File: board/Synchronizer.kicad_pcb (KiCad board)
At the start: 2 copper layers, 99 x 61 mm, 46 parts, among them J1 Conn_01x02_Socket, J2 COIL1, J3 COIL2, Q1 2N3904, Q2 2N3906, Q3 IRF9540N, Q4 2N3904, U1 Pico, U2 LM7805_TO220, U3 LM358

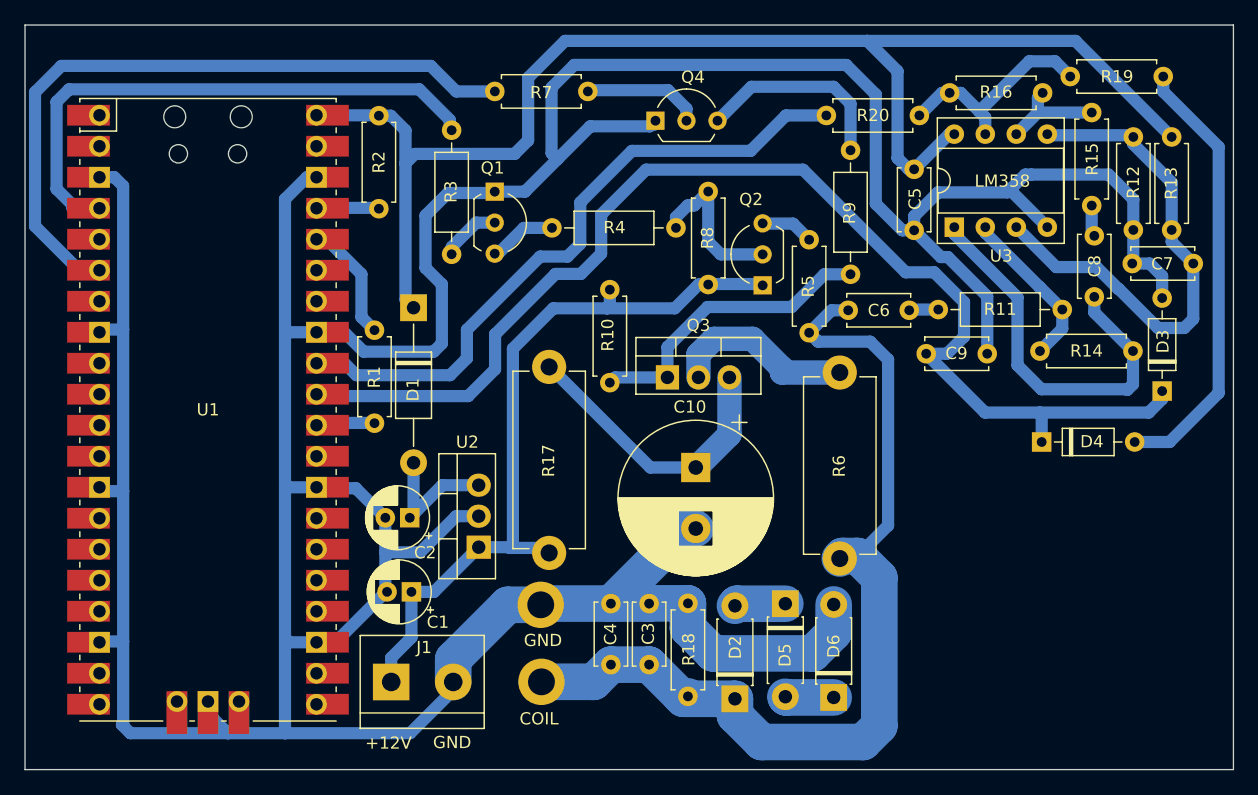
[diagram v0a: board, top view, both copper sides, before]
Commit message: Added pcb2gcode generation of gcode for mill
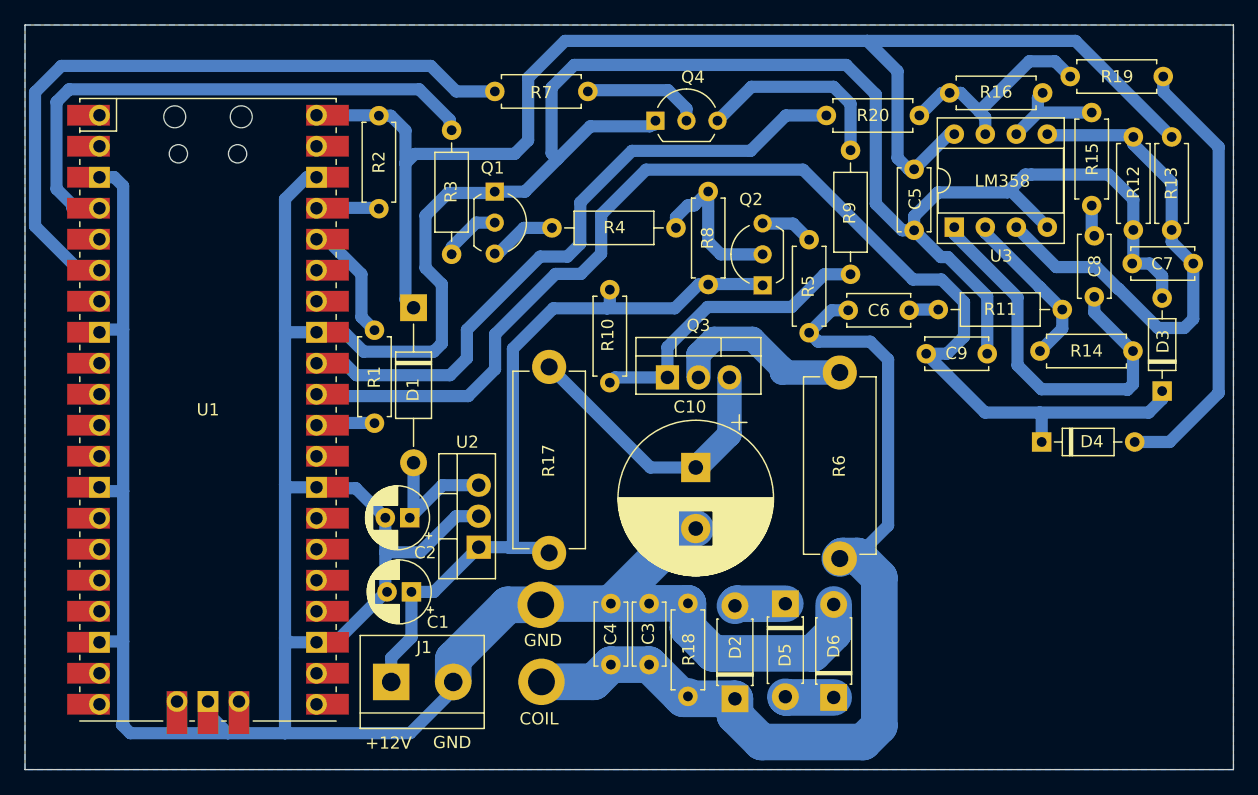
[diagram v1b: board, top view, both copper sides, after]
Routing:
- added copper zone on B.Cu, net (none)
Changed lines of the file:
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@@
   (segment (start 178.6 44.54) (end 181.77 47.71) (width 1) (layer "B.Cu") (net 9))
   (segment (start 181.77 50.43) (end 181.77 47.71) (width 1) (layer "B.Cu") (net 9))
-  (segment (start 134.46 41.39) (end 129.51 46.34) (width 1) (layer "B.Cu") (net 10))
-  (segment (start 129.51 46.34) (end 129.51 49.2) (width 1) (layer "B.Cu") (net 10))
+  (segment (start 115.03 51.4) (end 114.88 51.25) (width 1) (layer "B.Cu") (net 10))
   (segment (start 166.53 47.93) (end 167.93 46.53) (width 1) (layer "B.Cu") (net 10))
+  (segment (start 129.51 49.2) (end 127.31 51.4) (width 1) (layer "B.Cu") (net 10))
+  (segment (start 167.93 46.53) (end 167.93 43.7) (width 1) (layer "B.Cu") (net 10))
+  (segment (start 141.88 32.85) (end 138.2 36.53) (width 1) (layer "B.Cu") (net 10))
+  (segment (start 163.74 41.85) (end 154.74 32.85) (width 1) (layer "B.Cu") (net 10))
   (segment (start 164.83 47.93) (end 166.53 47.93) (width 1) (layer "B.Cu") (net 10))
-  (segment (start 115.03 51.4) (end 114.88 51.25) (width 1) (layer "B.Cu") (net 10))
-  (segment (start 127.31 51.4) (end 115.03 51.4) (width 1) (layer "B.Cu") (net 10))
   (segment (start 174.13 52.75) (end 169.65 52.75) (width 1) (layer "B.Cu") (net 10))
-  (segment (start 165.49 41.26) (end 163.15 41.26) (width 1) (layer "B.Cu") (net 10))
+  (segment (start 154.74 32.85) (end 141.88 32.85) (width 1) (layer "B.Cu") (net 10))
+  (segment (start 138.2 36.53) (end 138.2 39.73) (width 1) (layer "B.Cu") (net 10))
   (segment (start 169.65 52.75) (end 164.83 47.93) (width 1) (layer "B.Cu") (net 10))
-  (segment (start 154.74 32.85) (end 141.88 32.85) (width 1) (layer "B.Cu") (net 10))
-  (segment (start 167.93 43.7) (end 165.49 41.26) (width 1) (layer "B.Cu") (net 10))
-  (segment (start 167.93 46.53) (end 167.93 43.7) (width 1) (layer "B.Cu") (net 10))
   (segment (start 183.06 52.75) (end 174.13 52.75) (width 1) (layer "B.Cu") (net 10))
   (segment (start 184.16 50.99) (end 184.16 51.65) (width 1) (layer "B.Cu") (net 10))
-  (segment (start 129.51 49.2) (end 127.31 51.4) (width 1) (layer "B.Cu") (net 10))
-  (segment (start 138.2 36.53) (end 138.2 39.73) (width 1) (layer "B.Cu") (net 10))
-  (segment (start 141.88 32.85) (end 138.2 36.53) (width 1) (layer "B.Cu") (net 10))
-  (segment (start 163.15 41.26) (end 154.74 32.85) (width 1) (layer "B.Cu") (net 10))
   (segment (start 138.2 39.73) (end 136.54 41.39) (width 1) (layer "B.Cu") (net 10))
+  (segment (start 136.54 41.39) (end 134.46 41.39) (width 1) (layer "B.Cu") (net 10))
+  (segment (start 129.51 46.34) (end 129.51 49.2) (width 1) (layer "B.Cu") (net 10))
+  (segment (start 134.46 41.39) (end 129.51 46.34) (width 1) (layer "B.Cu") (net 10))
   (segment (start 184.16 51.65) (end 183.06 52.75) (width 1) (layer "B.Cu") (net 10))
   (segment (start 174.29 52.91) (end 174.29 55.16) (width 1) (layer "B.Cu") (net 10))
+  (segment (start 167.93 43.7) (end 166.08 41.85) (width 1) (layer "B.Cu") (net 10))
   (segment (start 174.13 52.75) (end 174.29 52.91) (width 1) (layer "B.Cu") (net 10))
-  (segment (start 136.54 41.39) (end 134.46 41.39) (width 1) (layer "B.Cu") (net 10))
+  (segment (start 127.31 51.4) (end 115.03 51.4) (width 1) (layer "B.Cu") (net 10))
+  (segment (start 166.08 41.85) (end 163.74 41.85) (width 1) (layer "B.Cu") (net 10))
   (segment (start 148.71 49.87) (end 148.71 54.55) (width 2) (layer "B.Cu") (net 11))
   (segment (start 133.99 49.01) (end 133.94 49.01) (width 1) (layer "B.Cu") (net 11))
@@
   (segment (start 169.175 28.075) (end 167.66 26.56) (width 1) (layer "B.Cu") (net 57))
   (segment (start 169.67 28.57) (end 169.175 28.075) (width 1) (layer "B.Cu") (net 57))
+  (zone (net 0) (net_name "") (layer "B.Cu") (hatch edge 0.5)
+    (connect_pads (clearance 0.75))
+    (min_thickness 0.75) (filled_areas_thickness no)
+    (fill yes (thermal_gap 0.75) (thermal_bridge_width 0.75) (island_removal_mode 1) (island_area_min 10))
+    (polygon
+      (pts
+        (xy 91 21)
+        (xy 190 21)
+        (xy 190 82)
+        (xy 91 82)
+      )
+    )
+  )
 )

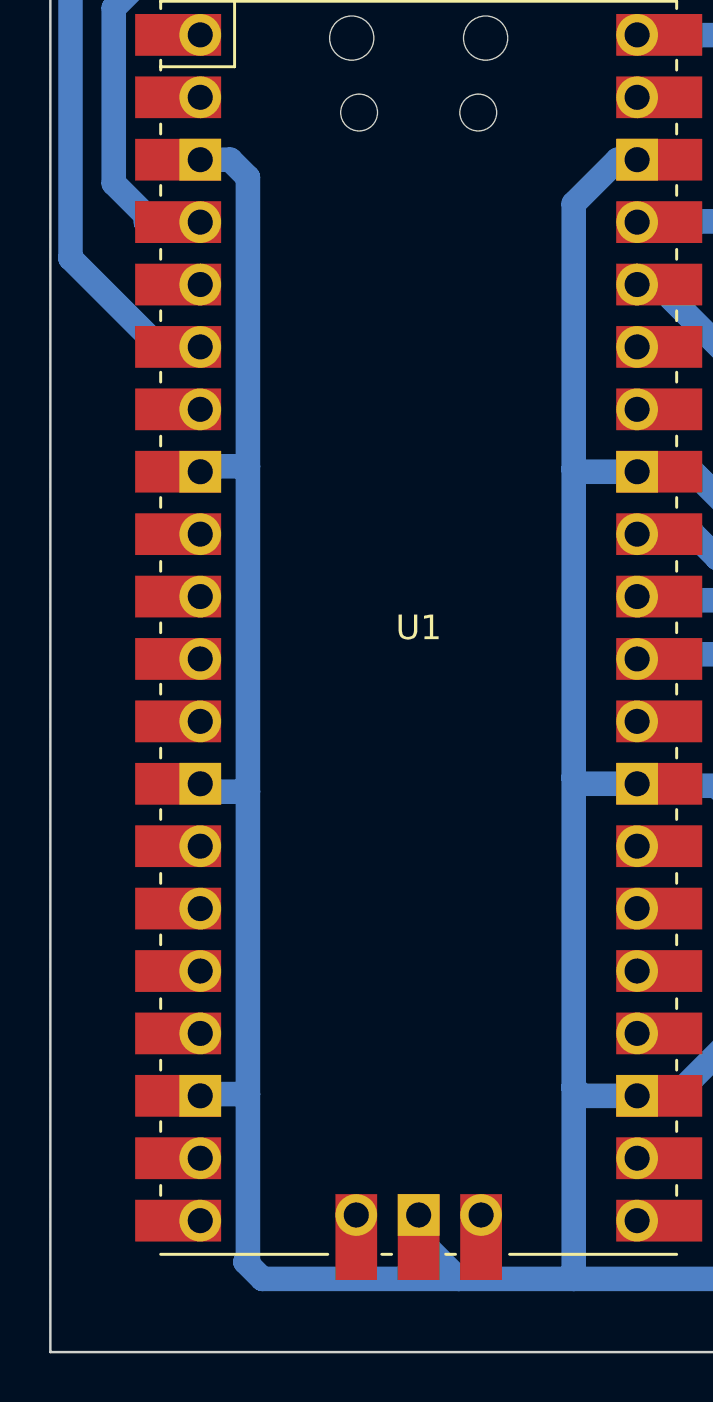
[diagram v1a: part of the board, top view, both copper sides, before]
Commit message: Added CAD of coil form
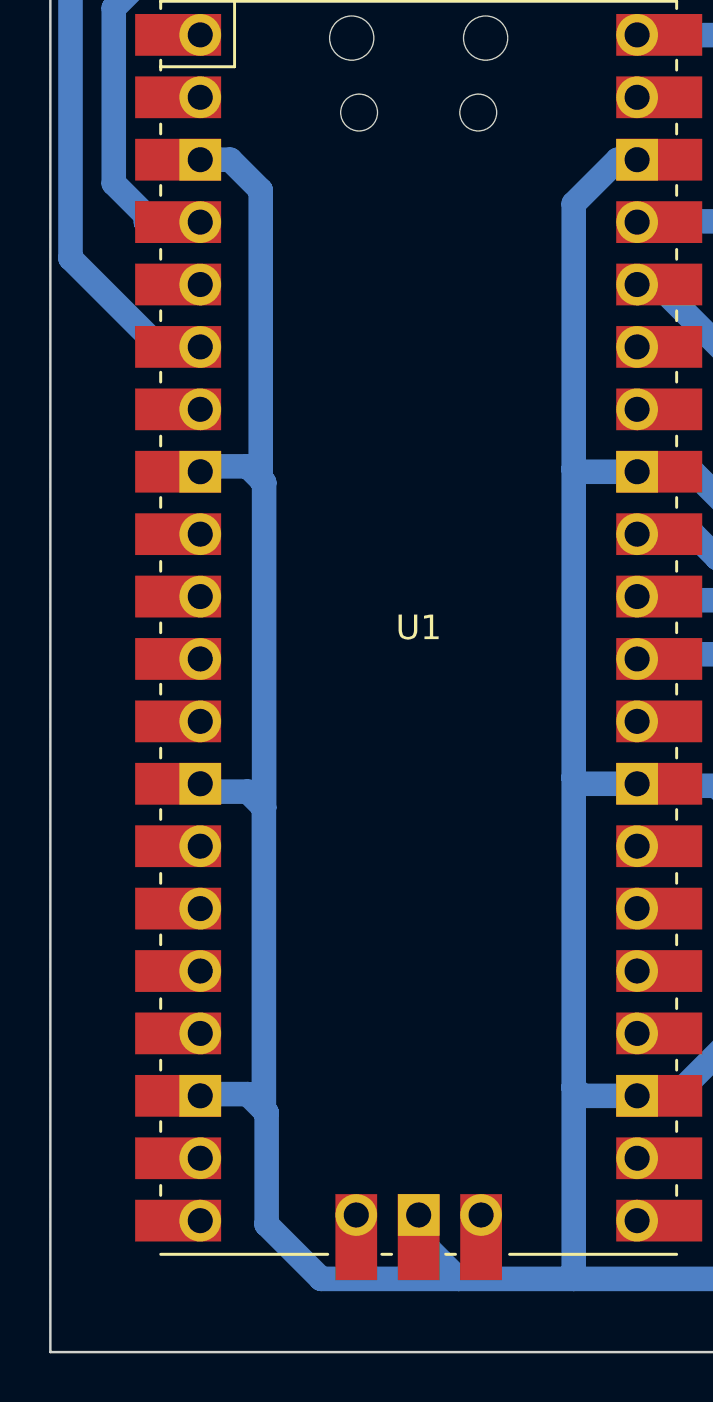
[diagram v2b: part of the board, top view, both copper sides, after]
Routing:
- net GND: track 360.6 -> 362.1 mm
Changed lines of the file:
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@@
   (segment (start 162.87 37.82) (end 163.84 37.82) (width 1) (layer "B.Cu") (net 2))
   (segment (start 137.31 29.3) (end 134.625 31.985) (width 1) (layer "B.Cu") (net 2))
-  (segment (start 99.04 78.23) (end 99.04 71.5) (width 1) (layer "B.Cu") (net 2))
   (segment (start 166.03 40.01) (end 163.84 37.82) (width 1) (layer "B.Cu") (net 2))
+  (segment (start 99.7 59.83) (end 99.7 46.61) (width 1) (layer "B.Cu") (net 2))
   (segment (start 169.83 47.93) (end 169.83 43.23) (width 1) (layer "B.Cu") (net 2))
   (segment (start 184.16 43.37) (end 184.16 41.56) (width 1) (layer "B.Cu") (net 2))
@@
   (segment (start 139 68.4) (end 133.35 68.4) (width 3) (layer "B.Cu") (net 2))
   (segment (start 133.35 68.4) (end 133.25 68.5) (width 3) (layer "B.Cu") (net 2))
-  (segment (start 99.04 59.19) (end 99.04 45.95) (width 1) (layer "B.Cu") (net 2))
   (segment (start 126.32 61.24) (end 128.17 61.24) (width 1) (layer "B.Cu") (net 2))
-  (segment (start 99.63 79.02) (end 98.94 78.33) (width 1) (layer "B.Cu") (net 2))
   (segment (start 173.44 33.25) (end 172.94 33.25) (width 1) (layer "B.Cu") (net 2))
   (segment (start 105.99 77.39) (end 107.62 79.02) (width 1) (layer "B.Cu") (net 2))
@@
   (segment (start 99.04 59.19) (end 97.42 59.19) (width 1) (layer "B.Cu") (net 2))
   (segment (start 145.31 68.38) (end 142.15 68.38) (width 3) (layer "B.Cu") (net 2))
+  (segment (start 99.8 72.26) (end 99.69 72.15) (width 1) (layer "B.Cu") (net 2))
   (segment (start 114.96 58.95) (end 114.88 58.87) (width 1) (layer "B.Cu") (net 2))
   (segment (start 123.81 40.9) (end 125.15 42.24) (width 1) (layer "B.Cu") (net 2))
@@
   (segment (start 181.8 37.79) (end 181.8 35.28) (width 1) (layer "B.Cu") (net 2))
   (segment (start 112.3 35.26) (end 114.09 33.47) (width 1) (layer "B.Cu") (net 2))
+  (segment (start 99.56 34.71) (end 98.32 33.47) (width 1) (layer "B.Cu") (net 2))
+  (segment (start 99.69 59.84) (end 99.7 59.83) (width 1) (layer "B.Cu") (net 2))
   (segment (start 157.25 68.47) (end 157.25 70.76) (width 3) (layer "B.Cu") (net 2))
   (segment (start 174.75 37.56) (end 171.69 34.5) (width 1) (layer "B.Cu") (net 2))
@@
   (segment (start 134.14 26.12) (end 135.99 24.27) (width 1) (layer "B.Cu") (net 2))
   (segment (start 184.16 41.56) (end 183.14 40.54) (width 1) (layer "B.Cu") (net 2))
+  (segment (start 99.7 46.61) (end 99.04 45.95) (width 1) (layer "B.Cu") (net 2))
   (segment (start 134.625 31.985) (end 131.96 34.65) (width 1) (layer "B.Cu") (net 2))
   (segment (start 155.53 72.48) (end 147.37 72.48) (width 3) (layer "B.Cu") (net 2))
   (segment (start 157.25 70.76) (end 155.53 72.48) (width 3) (layer "B.Cu") (net 2))
   (segment (start 112.3 71.23) (end 112.3 58.62) (width 1) (layer "B.Cu") (net 2))
-  (segment (start 98.32 33.47) (end 97.1 33.47) (width 1) (layer "B.Cu") (net 2))
+  (segment (start 99.56 46.47) (end 99.56 34.71) (width 1) (layer "B.Cu") (net 2))
   (segment (start 126.08 72.96) (end 126.08 74.82) (width 3) (layer "B.Cu") (net 2))
   (segment (start 126.08 75.49) (end 126.08 74.82) (width 1) (layer "B.Cu") (net 2))
@@
   (segment (start 114.88 71.57) (end 112.64 71.57) (width 1) (layer "B.Cu") (net 2))
   (segment (start 114.88 58.87) (end 112.55 58.87) (width 1) (layer "B.Cu") (net 2))
+  (segment (start 99.69 72.15) (end 99.69 59.84) (width 1) (layer "B.Cu") (net 2))
   (segment (start 112.55 58.87) (end 112.3 58.62) (width 1) (layer "B.Cu") (net 2))
   (segment (start 112.64 71.57) (end 112.3 71.23) (width 1) (layer "B.Cu") (net 2))
   (segment (start 114.88 46.17) (end 112.4 46.17) (width 1) (layer "B.Cu") (net 2))
+  (segment (start 102.02 79.02) (end 99.8 76.8) (width 1) (layer "B.Cu") (net 2))
   (segment (start 114.88 71.57) (end 116.43 71.57) (width 1) (layer "B.Cu") (net 2))
   (segment (start 142.13 68.4) (end 139 68.4) (width 3) (layer "B.Cu") (net 2))
   (segment (start 134.14 31.5) (end 134.14 26.12) (width 1) (layer "B.Cu") (net 2))
   (segment (start 145.15 62.25) (end 139 68.4) (width 3) (layer "B.Cu") (net 2))
+  (segment (start 99.8 76.8) (end 99.8 72.26) (width 1) (layer "B.Cu") (net 2))
   (segment (start 120.52 64.2) (end 123.36 64.2) (width 1) (layer "B.Cu") (net 2))
   (segment (start 118.1 58.95) (end 114.96 58.95) (width 1) (layer "B.Cu") (net 2))
   (segment (start 97.42 59.19) (end 97.1 58.87) (width 1) (layer "B.Cu") (net 2))
-  (segment (start 98.94 78.33) (end 99.04 78.23) (width 1) (layer "B.Cu") (net 2))
-  (segment (start 107.62 79.02) (end 99.63 79.02) (width 1) (layer "B.Cu") (net 2))
   (segment (start 129.48 34.65) (end 129.37 34.76) (width 1) (layer "B.Cu") (net 2))
+  (segment (start 99.8 72.26) (end 99.04 71.5) (width 1) (layer "B.Cu") (net 2))
   (segment (start 112.3 79.02) (end 112.3 71.23) (width 1) (layer "B.Cu") (net 2))
   (segment (start 114.09 33.47) (end 114.88 33.47) (width 1) (layer "B.Cu") (net 2))
-  (segment (start 99.04 34.19) (end 98.32 33.47) (width 1) (layer "B.Cu") (net 2))
-  (segment (start 99.04 45.95) (end 99.04 34.19) (width 1) (layer "B.Cu") (net 2))
   (segment (start 169.83 43.23) (end 166.61 40.01) (width 1) (layer "B.Cu") (net 2))
   (segment (start 142.19 29.3) (end 137.31 29.3) (width 1) (layer "B.Cu") (net 2))
   (segment (start 112.3 79.02) (end 122.55 79.02) (width 1) (layer "B.Cu") (net 2))
   (segment (start 173.44 33.25) (end 179.77 33.25) (width 1) (layer "B.Cu") (net 2))
+  (segment (start 107.62 79.02) (end 102.02 79.02) (width 1) (layer "B.Cu") (net 2))
   (segment (start 99.04 45.95) (end 97.32 45.95) (width 1) (layer "B.Cu") (net 2))
   (segment (start 116.43 71.57) (end 120.56 67.44) (width 1) (layer "B.Cu") (net 2))
   (segment (start 120.52 64.2) (end 120.52 67.3) (width 1) (layer "B.Cu") (net 2))
   (segment (start 112.4 46.17) (end 112.3 46.07) (width 1) (layer "B.Cu") (net 2))
+  (segment (start 99.7 46.61) (end 99.56 46.47) (width 1) (layer "B.Cu") (net 2))
   (segment (start 105.99 76.42) (end 105.99 77.39) (width 1) (layer "B.Cu") (net 2))
   (segment (start 160.7 26.69) (end 160.7 35.65) (width 1) (layer "B.Cu") (net 2))
   (segment (start 158.28 24.27) (end 160.7 26.69) (width 1) (layer "B.Cu") (net 2))
   (segment (start 166.61 40.01) (end 166.03 40.01) (width 1) (layer "B.Cu") (net 2))
+  (segment (start 98.32 33.47) (end 97.1 33.47) (width 1) (layer "B.Cu") (net 2))
   (segment (start 171.48 34.71) (end 165.8 34.71) (width 1) (layer "B.Cu") (net 2))
   (segment (start 97.17 71.5) (end 97.1 71.57) (width 1) (layer "B.Cu") (net 2))
   (segment (start 142.51 29.19) (end 142.65 29.05) (width 1) (layer "B.Cu") (net 2))
-  (segment (start 99.04 71.5) (end 99.04 59.19) (width 1) (layer "B.Cu") (net 2))
+  (segment (start 99.69 59.84) (end 99.04 59.19) (width 1) (layer "B.Cu") (net 2))
   (segment (start 165.8 34.71) (end 163.84 36.67) (width 1) (layer "B.Cu") (net 2))
   (segment (start 99.04 71.5) (end 97.17 71.5) (width 1) (layer "B.Cu") (net 2))

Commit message: added extra gpio pins
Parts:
- removed J3: COIL2, MountingHole:MountingHole_2.2mm_M2_DIN965_Pad
- added C11: 100 nF, Capacitor_THT:C_Disc_D5.0mm_W2.5mm_P5.00mm, F.Cu at (97.7, 32.8)
- added J4: Barrel_Jack_Switch, Connector_BarrelJack:BarrelJack_Horizontal, F.Cu at (45.9, 50.8)
- added J5: COIL, TerminalBlock:TerminalBlock_bornier-2_P5.08mm, F.Cu at (69.4, 42.0)
- added R21: 10k, Resistor_THT:R_Axial_DIN0207_L6.3mm_D2.5mm_P7.62mm_Horizontal, F.Cu at (82.6, 36.0)
- C10: footprint Capacitor_THT:CP_Radial_D12.5mm_P5.00mm -> Capacitor_THT:CP_Radial_D14.0mm_P5.00mm
- J1: value Conn_01x02_Socket -> POWER
- J2: value COIL1 -> Conn_01x14; footprint MountingHole:MountingHole_2.2mm_M2_DIN965_Pad -> Connector_PinHeader_2.54mm:PinHeader_1x14_P2.54mm_Vertical
- R18: value 10k -> NC
- R5: value 1k -> 10k
- moved J2 141.2 mm to (2.02, 22.8)
- moved D4 94.3 mm to (82.6, 33.1)
- moved C10 94.0 mm to (54.1, 37.3)
- moved C7 93.4 mm to (95.7, 19.5)
- moved C9 93.4 mm to (73.8, 26.9)
- moved R12 93.4 mm to (90.8, 16.8)
- moved R14 93.4 mm to (90.8, 26.7)
- moved R20 93.4 mm to (73.3, 7.41)
- moved R4 93.4 mm to (53.3, 16.6)
- moved R5 93.4 mm to (64.2, 17.6)
- moved R7 93.4 mm to (46.1, 5.44)
- moved C1 93.4 mm to (31.7, 46.4)
- moved C2 93.4 mm to (31.5, 40.4)
- moved C5 93.4 mm to (72.8, 11.8)
- moved C6 93.4 mm to (67.4, 23.4)
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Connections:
- D3 pad 1: /AMPLITUDE -> Net-(D3-K)
- D4 pad 2: Net-(D4-A) -> Net-(D3-K)
- J2 pad 1: Net-(D2-K) -> Net-(J2-Pin_1)
- R19 pad 2: Net-(D4-A) -> Net-(C11-Pad1)
- U1 pad 10: unconnected-(U1-GPIO7-Pad10) -> Net-(J2-Pin_4)
- U1 pad 11: unconnected-(U1-GPIO8-Pad11) -> Net-(J2-Pin_5)
- U1 pad 12: unconnected-(U1-GPIO9-Pad12) -> Net-(J2-Pin_6)
- U1 pad 14: unconnected-(U1-GPIO10-Pad14) -> Net-(J2-Pin_8)
- U1 pad 15: unconnected-(U1-GPIO11-Pad15) -> Net-(J2-Pin_9)
- U1 pad 16: unconnected-(U1-GPIO12-Pad16) -> Net-(J2-Pin_10)
- U1 pad 17: unconnected-(U1-GPIO13-Pad17) -> Net-(J2-Pin_11)
- U1 pad 19: unconnected-(U1-GPIO14-Pad19) -> Net-(J2-Pin_13)
- U1 pad 20: unconnected-(U1-GPIO15-Pad20) -> Net-(J2-Pin_14)
- U1 pad 7: unconnected-(U1-GPIO5-Pad7) -> Net-(J2-Pin_1)
- U1 pad 9: unconnected-(U1-GPIO6-Pad9) -> Net-(J2-Pin_3)
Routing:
- net GND: track 362.1 -> 416.8 mm
- net Net-(D4-A): track 36.3 -> 0.00 mm
- net Net-(C11-Pad1): track 0.00 -> 30.5 mm
- net +12V: track 61.8 -> 77.7 mm
- net /AMPLITUDE: track 100.3 -> 89.6 mm
- net Net-(D3-K): track 0.00 -> 5.61 mm
- net Net-(D2-K): track 77.5 -> 83.0 mm
- net Net-(J2-Pin_8): track 0.00 -> 4.13 mm
- net Net-(J2-Pin_6): track 0.00 -> 4.13 mm
- net Net-(J2-Pin_14): track 0.00 -> 4.13 mm
- net Net-(J2-Pin_4): track 0.00 -> 4.13 mm
- net Net-(J2-Pin_1): track 0.00 -> 4.13 mm
- net Net-(J2-Pin_9): track 0.00 -> 4.13 mm
- net Net-(J2-Pin_5): track 0.00 -> 4.13 mm
- net Net-(J2-Pin_3): track 0.00 -> 4.13 mm
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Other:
- board size 99 x 61 mm -> 99 x 62 mm
